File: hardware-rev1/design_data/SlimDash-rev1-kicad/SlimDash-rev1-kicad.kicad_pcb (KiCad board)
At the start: 2 copper layers, 157.1 x 131.5 mm, 138 parts, among them J1 AudioJack4, J2 AudioJack4, U1 TLV73333PDBV, U2 RP2040, U3 W25Q128JVS, Y1 Crystal_GND24

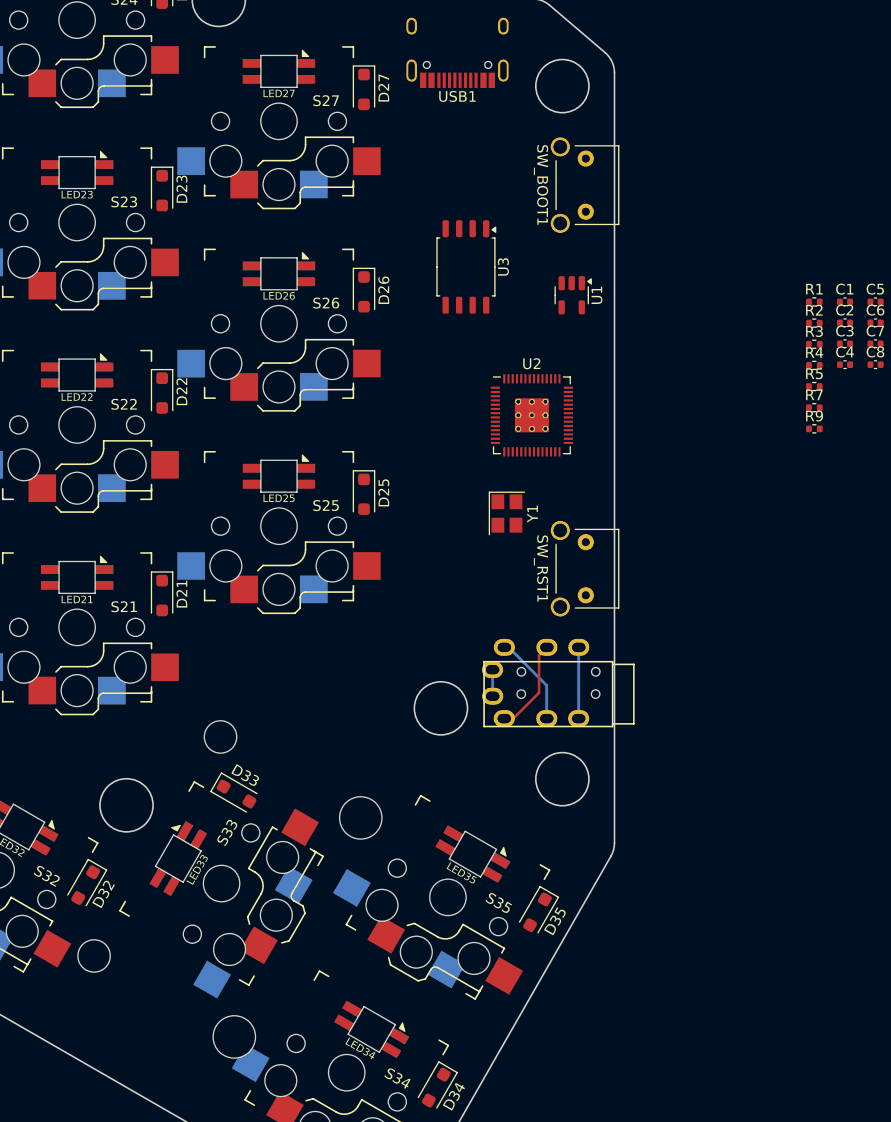
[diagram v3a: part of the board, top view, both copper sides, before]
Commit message: add surge protection
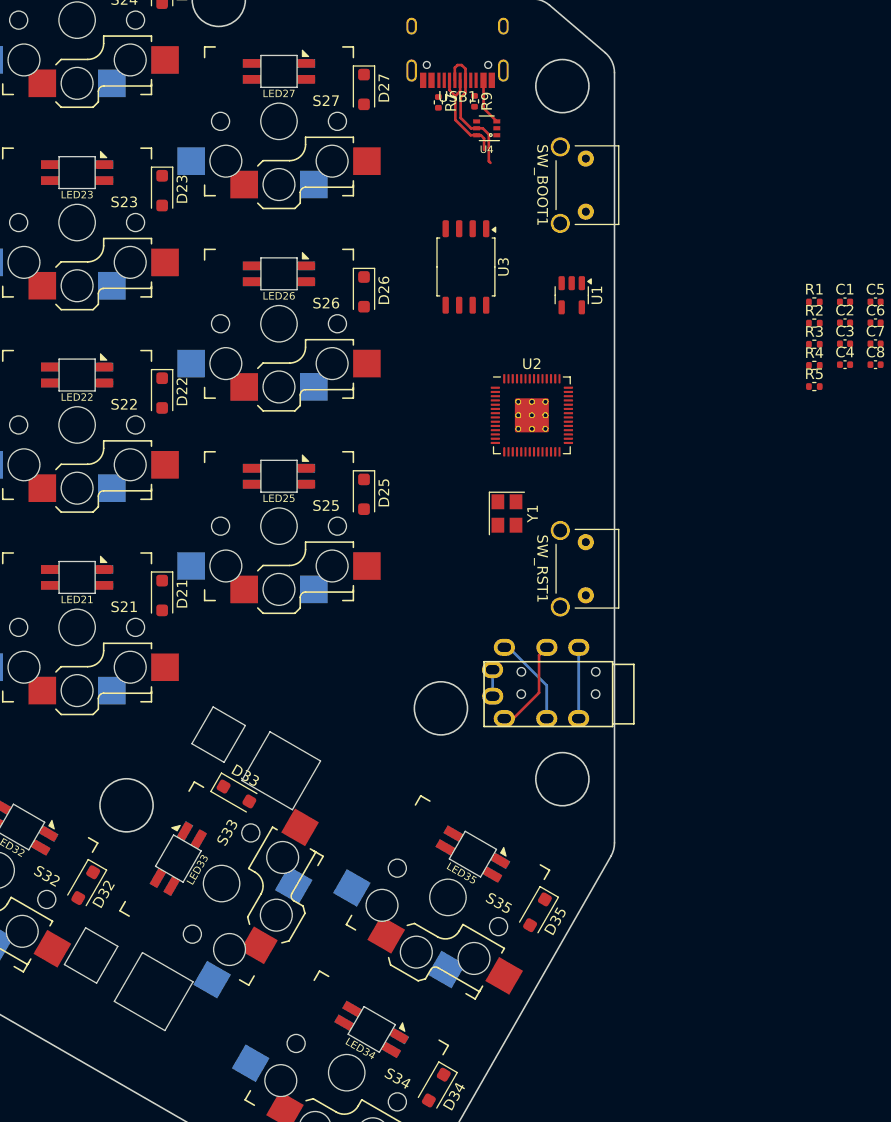
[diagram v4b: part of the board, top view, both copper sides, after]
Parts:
- removed REF**: Stabilizer_MX_2u, daprice_keyswitches:Stabilizer_MX_2u
- added Kailh PG1350_2U Stabilizer: Choc, mzm_misc:Kailh-PG1350-2u-stabilizer, F.Cu at (158.6, 121.7)
- added U4: ~, Keebio-Parts:SOT-363_SC-70-6, F.Cu at (183.6, 50.6)
- LED1, LED10, LED11, LED12, LED13, LED14, LED15, LED16, LED17, LED18, LED19, LED2, LED20, LED21, LED22, LED23, LED24, LED25, LED26, LED27, LED28, LED29, LED3, LED30, LED31, LED32, LED33, LED34, LED35, LED4, LED5, LED6, LED7, LED8, LED9: value (none) -> SK6812MINI-E
- moved R7 45.6 mm to (179.0, 48.2), turned to -90 degrees
- moved R9 44.4 mm to (182.4, 48.1), turned to -90 degrees
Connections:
- J1 pad 1: +3V3 -> +5V
- J2 pad 1: +3V3 -> +5V
- LED1 pad 1: +5V -> Net-(LED1-DOUT)
- LED1 pad 2: DOUT -> GND
- LED1 pad 3: GND -> Net-(LED1-DIN)
- LED1 pad 4: DIN -> +5V
- LED10 pad 1: +5V -> Net-(LED10-DOUT)
- LED10 pad 2: DOUT -> GND
- LED10 pad 3: GND -> Net-(LED10-DIN)
- LED10 pad 4: DIN -> +5V
- LED11 pad 1: +5V -> Net-(LED11-DOUT)
- LED11 pad 2: DOUT -> GND
- LED11 pad 3: GND -> Net-(LED11-DIN)
- LED11 pad 4: DIN -> +5V
- LED12 pad 1: +5V -> Net-(LED12-DOUT)
- LED12 pad 2: DOUT -> GND
- LED12 pad 3: GND -> Net-(LED12-DIN)
- LED12 pad 4: DIN -> +5V
- LED13 pad 1: +5V -> Net-(LED13-DOUT)
- LED13 pad 2: DOUT -> GND
- LED13 pad 3: GND -> Net-(LED13-DIN)
- LED13 pad 4: DIN -> +5V
- LED14 pad 1: +5V -> Net-(LED10-DIN)
- LED14 pad 2: DOUT -> GND
- LED14 pad 3: GND -> Net-(LED14-DIN)
- LED14 pad 4: DIN -> +5V
- LED15 pad 1: +5V -> Net-(LED15-DOUT)
- LED15 pad 2: DOUT -> GND
- LED15 pad 3: GND -> Net-(LED11-DOUT)
- LED15 pad 4: DIN -> +5V
- LED16 pad 1: +5V -> Net-(LED12-DIN)
- LED16 pad 2: DOUT -> GND
- LED16 pad 3: GND -> Net-(LED16-DIN)
- LED16 pad 4: DIN -> +5V
- LED17 pad 1: +5V -> Net-(LED17-DOUT)
- LED17 pad 2: DOUT -> GND
- LED17 pad 3: GND -> Net-(LED13-DOUT)
- LED17 pad 4: DIN -> +5V
- LED18 pad 1: +5V -> Net-(LED14-DIN)
- LED18 pad 2: DOUT -> GND
- LED18 pad 3: GND -> Net-(LED18-DIN)
- LED18 pad 4: DIN -> +5V
- LED19 pad 1: +5V -> Net-(LED19-DOUT)
- LED19 pad 2: DOUT -> GND
- LED19 pad 3: GND -> Net-(LED15-DOUT)
- LED19 pad 4: DIN -> +5V
- LED2 pad 1: +5V -> Net-(LED2-DOUT)
- LED2 pad 2: DOUT -> GND
- LED2 pad 3: GND -> Net-(LED2-DIN)
- LED2 pad 4: DIN -> +5V
- LED20 pad 1: +5V -> Net-(LED16-DIN)
- LED20 pad 2: DOUT -> GND
- LED20 pad 3: GND -> Net-(LED20-DIN)
- LED20 pad 4: DIN -> +5V
- LED21 pad 1: +5V -> Net-(LED21-DOUT)
- LED21 pad 2: DOUT -> GND
- LED21 pad 3: GND -> Net-(LED17-DOUT)
- LED21 pad 4: DIN -> +5V
- LED22 pad 1: +5V -> Net-(LED18-DIN)
- LED22 pad 2: DOUT -> GND
- LED22 pad 3: GND -> Net-(LED22-DIN)
- LED22 pad 4: DIN -> +5V
- LED23 pad 1: +5V -> Net-(LED23-DOUT)
- LED23 pad 2: DOUT -> GND
- LED23 pad 3: GND -> Net-(LED19-DOUT)
- LED23 pad 4: DIN -> +5V
- LED24 pad 1: +5V -> Net-(LED20-DIN)
- LED24 pad 2: DOUT -> GND
- LED24 pad 3: GND -> Net-(LED24-DIN)
- LED24 pad 4: DIN -> +5V
- LED25 pad 1: +5V -> Net-(LED25-DOUT)
- LED25 pad 2: DOUT -> GND
- LED25 pad 3: GND -> Net-(LED21-DOUT)
- LED25 pad 4: DIN -> +5V
- LED26 pad 1: +5V -> Net-(LED22-DIN)
- LED26 pad 2: DOUT -> GND
- LED26 pad 3: GND -> Net-(LED25-DOUT)
- LED26 pad 4: DIN -> +5V
- LED27 pad 1: +5V -> Net-(LED24-DIN)
- LED27 pad 2: DOUT -> GND
- LED27 pad 3: GND -> Net-(LED23-DOUT)
- LED27 pad 4: DIN -> +5V
- LED28 pad 1: +5V -> Net-(LED1-DIN)
- LED28 pad 2: DOUT -> GND
- LED28 pad 3: GND -> Net-(LED28-DIN)
- LED28 pad 4: DIN -> +5V
- LED29 pad 1: +5V -> Net-(LED28-DIN)
- LED29 pad 2: DOUT -> GND
- LED29 pad 3: GND -> Net-(LED29-DIN)
- LED29 pad 4: DIN -> +5V
- LED3 pad 1: +5V -> Net-(LED3-DOUT)
- LED3 pad 2: DOUT -> GND
- LED3 pad 3: GND -> Net-(LED2-DOUT)
- LED3 pad 4: DIN -> +5V
- LED30 pad 1: +5V -> Net-(LED29-DIN)
- LED30 pad 2: DOUT -> GND
- LED30 pad 3: GND -> Net-(LED30-DIN)
- LED30 pad 4: DIN -> +5V
- LED31 pad 1: +5V -> Net-(LED30-DIN)
- LED31 pad 2: DOUT -> GND
- LED31 pad 3: GND -> Net-(LED31-DIN)
- LED31 pad 4: DIN -> +5V
- LED32 pad 1: +5V -> Net-(LED31-DIN)
- LED32 pad 2: DOUT -> GND
- LED32 pad 3: GND -> Net-(LED32-DIN)
- LED32 pad 4: DIN -> +5V
- LED33 pad 1: +5V -> Net-(LED32-DIN)
- LED33 pad 2: DOUT -> GND
- LED33 pad 3: GND -> Net-(LED33-DIN)
- LED33 pad 4: DIN -> +5V
- LED34 pad 1: +5V -> Net-(LED33-DIN)
- LED34 pad 2: DOUT -> GND
- LED34 pad 3: GND -> Net-(LED34-DIN)
- LED34 pad 4: DIN -> +5V
- LED35 pad 1: +5V -> Net-(LED34-DIN)
- LED35 pad 2: DOUT -> GND
- LED35 pad 3: GND -> DIN
- LED35 pad 4: DIN -> +5V
- LED4 pad 1: +5V -> unconnected-(LED4-DOUT-Pad1)_1
- LED4 pad 2: DOUT -> GND
- LED4 pad 3: GND -> Net-(LED4-DIN)
- LED4 pad 4: DIN -> +5V
- LED5 pad 1: +5V -> Net-(LED5-DOUT)
- LED5 pad 2: DOUT -> GND
- LED5 pad 3: GND -> Net-(LED1-DOUT)
- LED5 pad 4: DIN -> +5V
- LED6 pad 1: +5V -> Net-(LED2-DIN)
- LED6 pad 2: DOUT -> GND
- LED6 pad 3: GND -> Net-(LED10-DOUT)
- LED6 pad 4: DIN -> +5V
- LED7 pad 1: +5V -> Net-(LED11-DIN)
- LED7 pad 2: DOUT -> GND
- LED7 pad 3: GND -> Net-(LED3-DOUT)
- LED7 pad 4: DIN -> +5V
- LED8 pad 1: +5V -> Net-(LED4-DIN)
- LED8 pad 2: DOUT -> GND
- LED8 pad 3: GND -> Net-(LED12-DOUT)
- LED8 pad 4: DIN -> +5V
- LED9 pad 1: +5V -> Net-(LED13-DIN)
- LED9 pad 2: DOUT -> GND
- LED9 pad 3: GND -> Net-(LED5-DOUT)
- LED9 pad 4: DIN -> +5V
- U2 pad 28: unconnected-(U2-GPIO17-Pad28) -> PIO_TX
- U2 pad 29: unconnected-(U2-GPIO18-Pad29) -> PIO_RX
- U2 pad 31: unconnected-(U2-GPIO20-Pad31) -> DIN
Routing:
- net USB_DM: track 0.00 -> 13.3 mm
- net USB_DP: track 0.00 -> 10.1 mm
- net +5V: track 0.00 -> 6.89 mm
- net +3V3: track 2.51 -> 0.00 mm

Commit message: trace routing progress
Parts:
- added JP1: SolderJumper_2_Open, Jumper:SolderJumper-2_P1.3mm_Open_RoundedPad1.0x1.5mm, F.Cu at (185.8, 111.3)
- moved C15 45.1 mm to (181.4, 78.2), turned to 180 degrees
- moved C14 43.9 mm to (182.3, 73.9), turned to 90 degrees
- moved C16 40.1 mm to (187.1, 83.3), turned to -90 degrees
- moved C11 39.5 mm to (187.4, 87.9), turned to -90 degrees
- moved C8 37.9 mm to (184.1, 84.7)
- moved C12 37.6 mm to (185.6, 69.1), turned to -90 degrees
- moved R4 36.8 mm to (181.7, 56.0), turned to 180 degrees
- moved C13 34.4 mm to (192.1, 73.5)
- moved R5 33.9 mm to (184.1, 59.8), turned to -90 degrees
- moved C10 33.2 mm to (190.0, 72.1), turned to 90 degrees
- moved R1 33.1 mm to (186.0, 84.1), turned to 90 degrees
- moved C7 32.6 mm to (187.6, 70.1), turned to 90 degrees
- moved C9 31.8 mm to (192.1, 74.5)
- moved C4 31.0 mm to (188.1, 83.3), turned to -90 degrees
- moved C1 30.8 mm to (186.6, 70.1), turned to 90 degrees
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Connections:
- LED35 pad 3: DIN -> Net-(JP1-B)
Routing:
- net COL0: track 0.00 -> 307.4 mm, vias 0 -> 6
- net COL2: track 0.00 -> 246.9 mm, vias 0 -> 5
- net COL1: track 0.00 -> 235.8 mm, vias 0 -> 6
- net COL3: track 0.00 -> 227.5 mm, vias 0 -> 5
- net COL4: track 0.00 -> 206.7 mm, vias 0 -> 5
- net COL5: track 0.00 -> 198.0 mm, vias 0 -> 5
- net COL6: track 0.00 -> 171.7 mm, vias 0 -> 4
- net +5V: track 6.89 -> 93.2 mm, vias 0 -> 1
- net +3V3: track 0.00 -> 68.9 mm
- net Net-(R4-Pad2): track 0.00 -> 48.1 mm, vias 0 -> 1
- net DIN: track 0.00 -> 38.2 mm
- net GND: track 6.71 -> 43.3 mm, vias 0 -> 25
- net QSPI_SS: track 0.00 -> 30.3 mm, vias 0 -> 2
- net Net-(D32-A): track 0.00 -> 25.6 mm, vias 0 -> 1
- net QSPI_SD1: track 0.00 -> 25.0 mm
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- added copper zone on F.Cu, net +1V1
- added copper zone on F.Cu, net +3V3
- added copper zone on F.Cu, net +5V
- added copper zone on B.Cu, net GND
- added copper zone on F.Cu, net GND
